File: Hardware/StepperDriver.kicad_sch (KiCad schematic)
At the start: 0 parts

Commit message: Initial schematic
Completed the first iteration for the schematic.
Included a default 42x42mm PCB area.
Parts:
- added C1, C3, C4: 22u, Capacitor_SMD:C_1206_3216Metric, symbol Device:C
- added C10, C11, C15, C16, C17, C18, C20, C21, C6, C9: 100n, Capacitor_SMD:C_0603_1608Metric, symbol Device:C
- added C12, C19, C2, C8: 10n, Capacitor_SMD:C_0603_1608Metric, symbol Device:C
- added C13: 2.2u, Capacitor_SMD:C_0603_1608Metric, symbol Device:C
- added C14: 100u, Capacitor_SMD:CP_Elec_8x10.5, symbol Device:C_Polarized
- added C5: 22n, Capacitor_SMD:C_0603_1608Metric, symbol Device:C
- added C7: 1u, Capacitor_SMD:C_0603_1608Metric, symbol Device:C
- added D1, D2: SS210, Diode_SMD:D_SMA, symbol Device:D_Schottky
- added J1: LCD, Custom_Parts:OLED_128X32_0.91, symbol Connector_Generic:Conn_01x04
- added J2: JTAG, Connector_PinHeader_1.27mm:PinHeader_2x05_P1.27mm_Vertical, symbol Connector:Conn_ARM_JTAG_SWD_10
- added J3: UART, Connector_JST:JST_SH_SM03B-SRSS-TB_1x03-1MP_P1.00mm_Horizontal, symbol Connector_Generic_MountingPin:Conn_01x03_MountingPin
- added J4: MOTOR, Connector_PinHeader_2.54mm:PinHeader_1x04_P2.54mm_Vertical, symbol Connector_Generic:Conn_01x04
- added L1: 47u, Inductor_SMD:L_Changjiang_FNR5040S, symbol Device:L
- added R1, R2: 2.2K, Resistor_SMD:R_0603_1608Metric, symbol Device:R
- added R10, R12, R13, R15, R16, R6, R9: 10K, Resistor_SMD:R_0603_1608Metric, symbol Device:R
- added R11, R14: 100m, Resistor_SMD:R_1206_3216Metric, symbol Device:R
- added R3, R4: 100, Resistor_SMD:R_0603_1608Metric, symbol Device:R
- added R5: 1K, Resistor_SMD:R_0603_1608Metric, symbol Device:R
- added R7: 3.3K, Resistor_SMD:R_0603_1608Metric, symbol Device:R
- added R8: 22K, Resistor_SMD:R_0603_1608Metric, symbol Device:R
- added SW1: SW_M, Button_Switch_SMD:SW_SPST_TS-1088-xR020, symbol Switch:SW_Push
- added SW2: SW_C, Button_Switch_SMD:SW_SPST_TS-1088-xR020, symbol Switch:SW_Push
- added SW3: SW_P, Button_Switch_SMD:SW_SPST_TS-1088-xR020, symbol Switch:SW_Push
- added U1: TPS5430DDA, Custom_Parts:TI_SO-PowerPAD-8_ThermalVias, symbol Regulator_Switching:TPS5430DDA
- added U2: XIAO-RP2350, Custom_Parts:XIAO-RP2350-SMD, symbol Custom_Parts:XIAO-RP2350-SMD
- added U3: TMC2208-LA, Custom_Parts:QFN-28-1EP_5x5mm_P0.5mm_EP3.1x3.1mm_ThermalVias, symbol Driver_Motor:TMC2208-LA
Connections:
- new net: R12.2, R13.2, SW2.1
- new net: R15.2, R16.2, SW3.1
- new net: R10.2, R9.2, SW1.1
- new net +3V3: C9.1, J1.3 (Pin_3), J2.1 (VTref), R1.1, R10.1, R13.1, R16.1, R2.1, U2.12 (3V3), U2.26 (3V3), U3.15 (VCC_IO)
- new net +5V: C3.1, C4.1, L1.2, R6.1, U2.14 (VBUS)
- new net +VDC: C10.1, C11.1, C14.1, C6.1, D1.2 (A), U3.22 (VS), U3.28 (VS)
- new net BOOT: C2.1, U1.1 (BOOT)
- new net CLK: J2.4 (SWCLK/TCK), R3.2
- new net CPI: C5.2, U3.5 (CPI)
- new net CPO: C5.1, U3.4 (CPO)
- new net DIO: J2.2 (SWDIO/TMS), R4.1
- new net DRV_DIAG: U2.18 (GPIO16_SDA0), U3.11 (DIAG)
- new net DRV_DIR: U2.1 (GPIO26_A0), U3.19 (DIR)
- new net DRV_EN: U2.4 (GPIO5_SPI0_CS), U3.2 (~{EN})
- new net DRV_INDEX: U2.17 (GPIO17_SCL0), U3.12 (INDEX)
- new net DRV_STEP: U2.2 (GPIO27_A1), U3.16 (STEP)
- new net DRV_UART: R5.1, U2.8 (GPIO1_RX0), U3.14 (~{PD}/UART)
- new net DRV_VREF: R8.1, U2.3 (GPIO28_A2)
- new net GND: C1.2, C10.2, C11.2, C12.2, C13.2, C14.2, C15.2, C16.2, C17.2, C18.2, C19.2, C20.2, C21.2, C3.2, C4.2, C7.2, C8.2, C9.2, D2.2 (A), J1.4 (Pin_4), J2.3 (GND), J2.5 (GND), J2.9 (GNDDetect), J3.2 (Pin_2), R11.2, R14.2, R7.2, SW1.2, SW2.2, SW3.2, U1.6 (GND), U1.9 (GNDPAD), U2.13 (GND), U2.27 (GND), U2.30 (GND), U3.13 (CLK), U3.18 (GND), U3.29 (GND), U3.3 (GND)
- new net M_A1: C15.1, J4.4 (Pin_4), U3.24 (OA1)
- new net M_A2: C17.1, J4.3 (Pin_3), U3.21 (OA2)
- new net M_B1: C18.1, J4.2 (Pin_2), U3.26 (OB1)
- new net M_B2: C20.1, J4.1 (Pin_1), U3.1 (OB2)
- new net RST: J2.10 (~{RESET}), U2.24 (RST)
- new net SCL: J1.2 (Pin_2), R1.2, U2.6 (GPIO7_SCL1)
- new net SDA: J1.1 (Pin_1), R2.2, U2.5 (GPIO6_SDA1)
- new net SNSA: C16.1, R11.1, U3.23 (BRA)
- new net SNSB: C21.1, R14.1, U3.27 (BRB)
- new net SWCLK: R3.1, U2.28 (SWDCLK)
- new net SWDIO: R4.2, U2.23 (SWDIO)
- new net SW_C: C12.1, R12.1, U2.10 (GPIO4_SPI0_MISO)
- new net SW_M: C8.1, R9.1, U2.9 (GPIO2_SPI0_SCK)
- new net SW_P: C19.1, R15.1, U2.11 (GPIO3_SPI0_MOSI)
- new net TX: R5.2, U2.7 (GPIO0_TXO)
- new net UART_RX: J3.1 (Pin_1), U2.15 (GPIO21_RX1)
- new net UART_TX: J3.3 (Pin_3), U2.16 (GPIO20_TX1)
- new net VCP: C6.2, U3.6 (VCP)
- new net VDC_PROT: C1.1, D1.1 (K), U1.7 (VIN)
- new net VOUT: C13.1, U3.8 (5VOUT)
- new net VREF: C7.1, R8.2, U3.17 (VREF)
- new net VSNS: R6.2, R7.1, U1.4 (VSENSE)
- new net VSW: C2.2, D2.1 (K), L1.1, U1.8 (PH)
- no-connect marks 0 -> 12

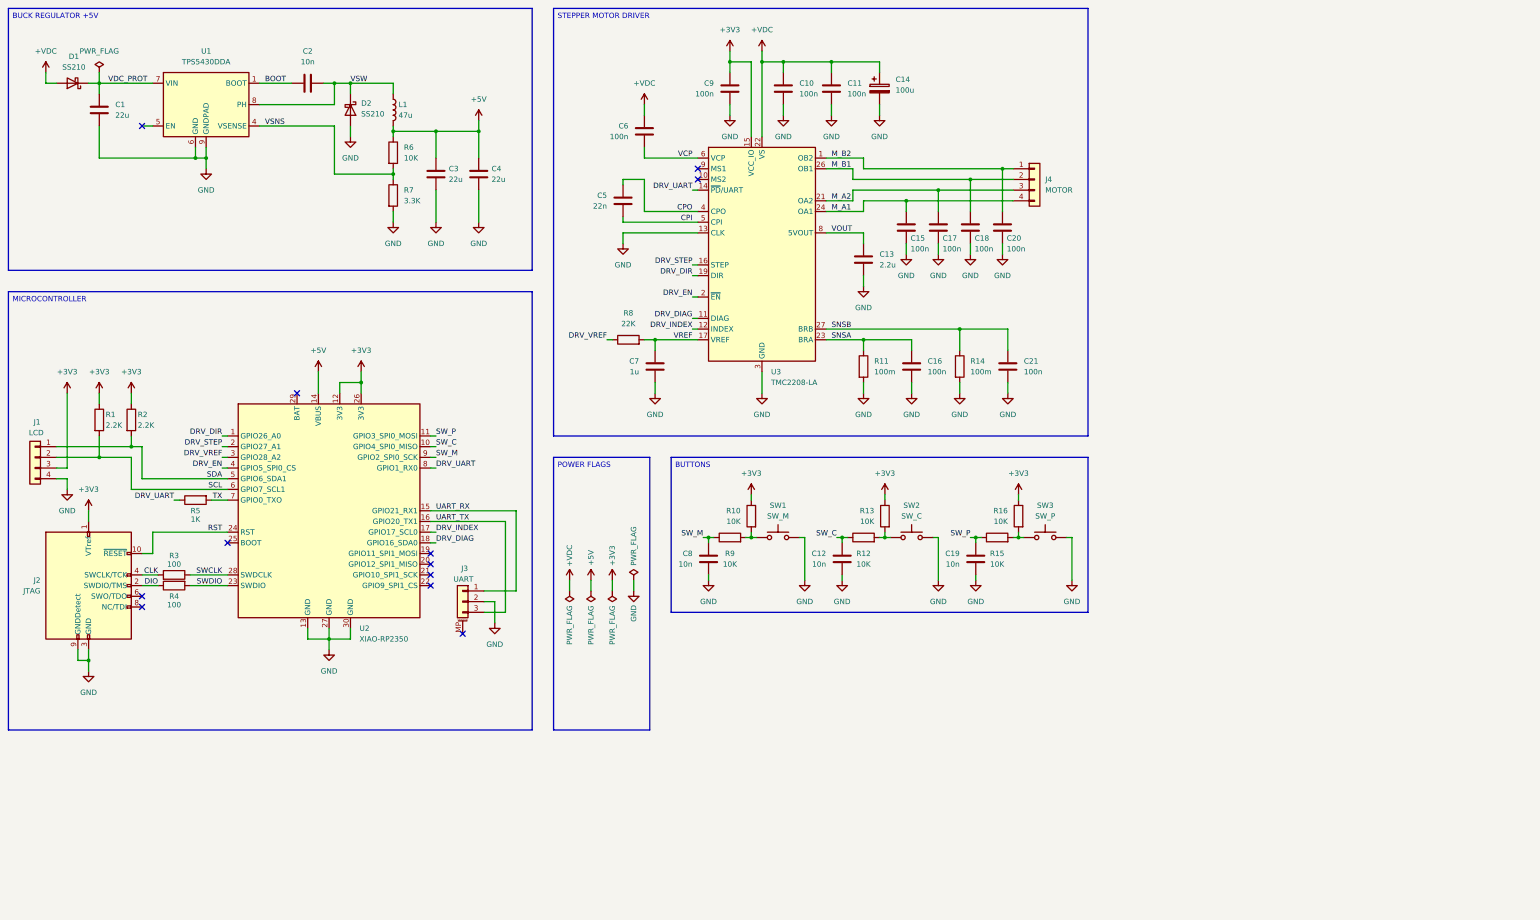
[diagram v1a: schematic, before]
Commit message: Initial layout
Completed the first iteration for the layout.
Increased the PCB area to 50x50mm.
Minor changes in the schematic.
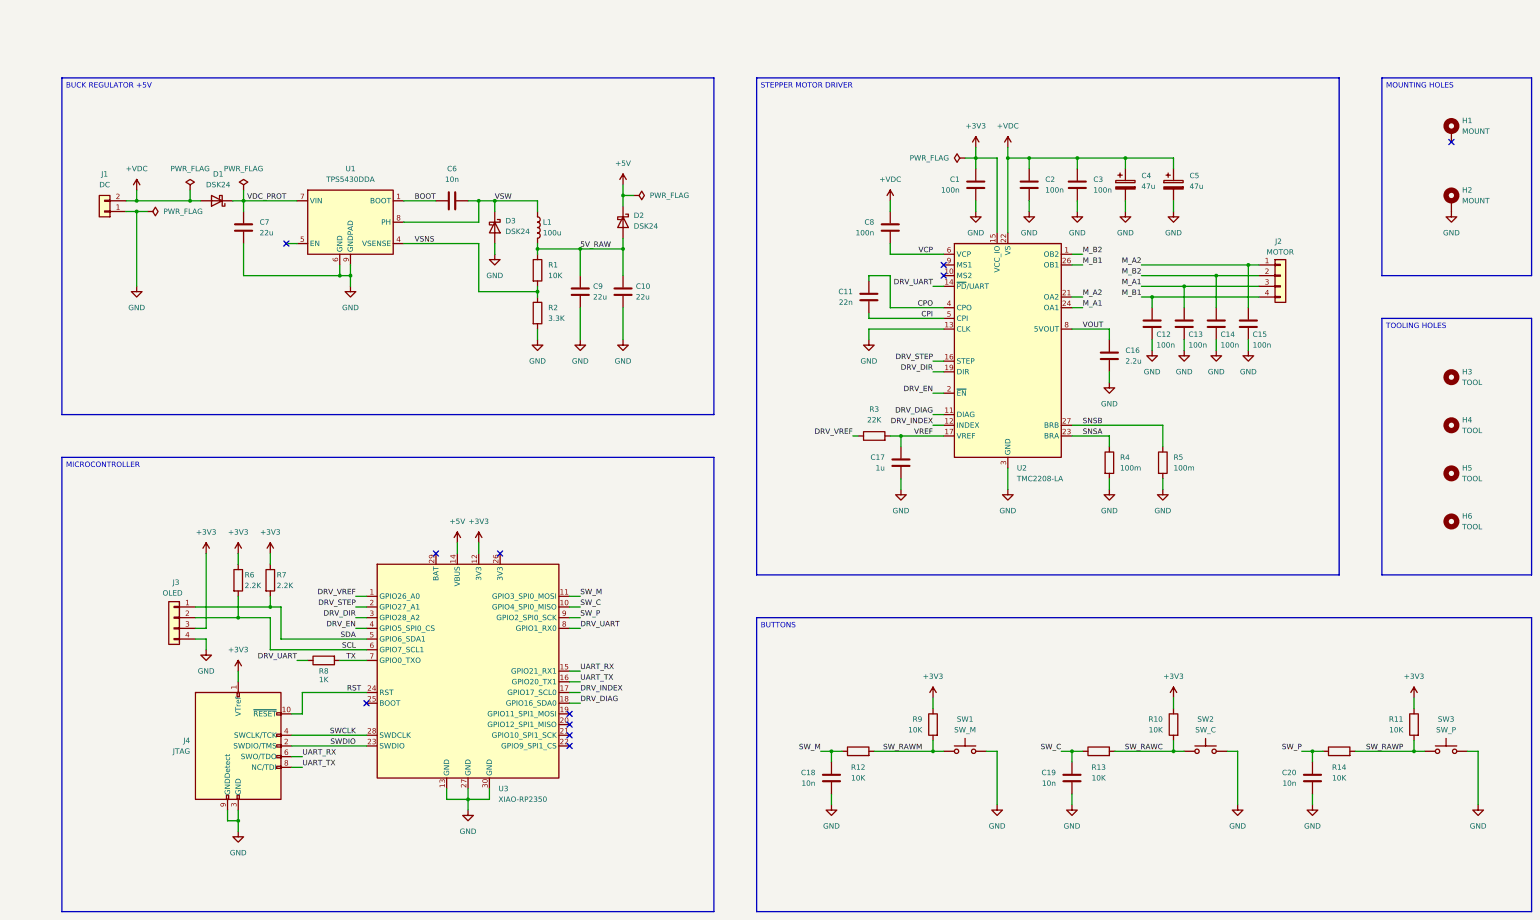
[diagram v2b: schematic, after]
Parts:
- removed C16, C21: 100n, Capacitor_SMD:C_0603_1608Metric, symbol Device:C
- removed J3: UART, Connector_JST:JST_SH_SM03B-SRSS-TB_1x03-1MP_P1.00mm_Horizontal, symbol Connector_Generic_MountingPin:Conn_01x03_MountingPin
- removed R3, R4: 100, Resistor_SMD:R_0603_1608Metric, symbol Device:R
- added C5: 47u, Capacitor_SMD:CP_Elec_6.3x5.4, symbol Device:C_Polarized
- added D2: DSK24, Diode_SMD:D_SOD-123F, symbol Device:D_Schottky
- added H1, H2: MOUNT, MountingHole:MountingHole_3.2mm_M3_Pad_Via, symbol Mechanical:MountingHole_Pad
- added H3, H4, H5, H6: TOOL, MountingHole:ToolingHole_1.152mm, symbol Mechanical:MountingHole
- added J1: DC, Custom_Parts:JST_PH_S2B_1x02_COMBO, symbol Connector_Generic:Conn_01x02
- C4: renamed from C14; value 100u -> 47u; footprint Capacitor_SMD:CP_Elec_8x10.5 -> Capacitor_SMD:CP_Elec_6.3x5.4
- D1: value SS210 -> DSK24; footprint Diode_SMD:D_SMA -> Diode_SMD:D_SOD-123F
- D3: renamed from D2; value SS210 -> DSK24; footprint Diode_SMD:D_SMA -> Diode_SMD:D_SOD-123F
- J2: renamed from J4; footprint Connector_PinHeader_2.54mm:PinHeader_1x04_P2.54mm_Vertical -> Custom_Parts:JST_PH_S4B_1x04_COMBO
- J3: renamed from J1; value LCD -> OLED; footprint Custom_Parts:OLED_128X32_0.91 -> Custom_Parts:OLED_128X32_0.91_HEADER
- L1: value 47u -> 100u
- renumbered C9 to C1, C4 to C10, C5 to C11, C15 to C12, C17 to C13, C18 to C14, C20 to C15, C13 to C16, C7 to C17, C8 to C18, C12 to C19, C10 to C2, C19 to C20, C11 to C3, C2 to C6, C1 to C7, C6 to C8, C3 to C9, J2 to J4, R6 to R1, R13 to R10, R16 to R11, R9 to R12, R12 to R13, R15 to R14, R7 to R2, R8 to R3, R11 to R4, R14 to R5, R1 to R6, R2 to R7, R5 to R8, R10 to R9, U3 to U2, U2 to U3
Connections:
- net CLK is gone; now on net SWCLK: J4.4 (SWCLK/TCK)
- net DIO is gone; now on net SWDIO: J4.2 (SWDIO/TMS)
- net +3V3: no longer U3.26 (3V3)
- net +5V: now also D2.1 (K); no longer C10.1, C9.1, L1.2, R1.1
- net +VDC: now also C5.1, J1.2 (Pin_2)
- net DRV_DIR: now also U3.3 (GPIO28_A2); no longer U3.1 (GPIO26_A0)
- net DRV_VREF: now also U3.1 (GPIO26_A0); no longer U3.3 (GPIO28_A2)
- net GND: now also C5.2, H2.1, J1.1 (Pin_1)
- net M_A1: now also C13.1, J2.3 (Pin_3); no longer C12.1, J2.4 (Pin_4)
- net M_A2: now also C15.1, J2.1 (Pin_1); no longer C13.1, J2.3 (Pin_3)
- net M_B1: now also C12.1, J2.4 (Pin_4); no longer C14.1, J2.2 (Pin_2)
- net M_B2: now also C14.1, J2.2 (Pin_2); no longer C15.1, J2.1 (Pin_1)
- net SW_M: now also U3.11 (GPIO3_SPI0_MOSI); no longer U3.9 (GPIO2_SPI0_SCK)
- net SW_P: now also U3.9 (GPIO2_SPI0_SCK); no longer U3.11 (GPIO3_SPI0_MOSI)
- net UART_RX: now also J4.6 (SWO/TDO)
- net UART_TX: now also J4.8 (NC/TDI)
- net SW_RAWC: now reaches R10.2, R13.2, SW2.1
- net SW_RAWP: now reaches R11.2, R14.2, SW3.1
- net SW_RAWM: now reaches R12.2, R9.2, SW1.1
- new net 5V_RAW: C10.1, C9.1, D2.2 (A), L1.2, R1.1
- no-connect marks 12 -> 11
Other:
- moved on the sheet: C1, C10, C11, C12, C13, C14, C15, C16, C17, C18, C19, C2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

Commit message: Initial ESP32C6 layout
Moved to a XIAO ESP32C6 development board.
Completed the first iteration for the layout.
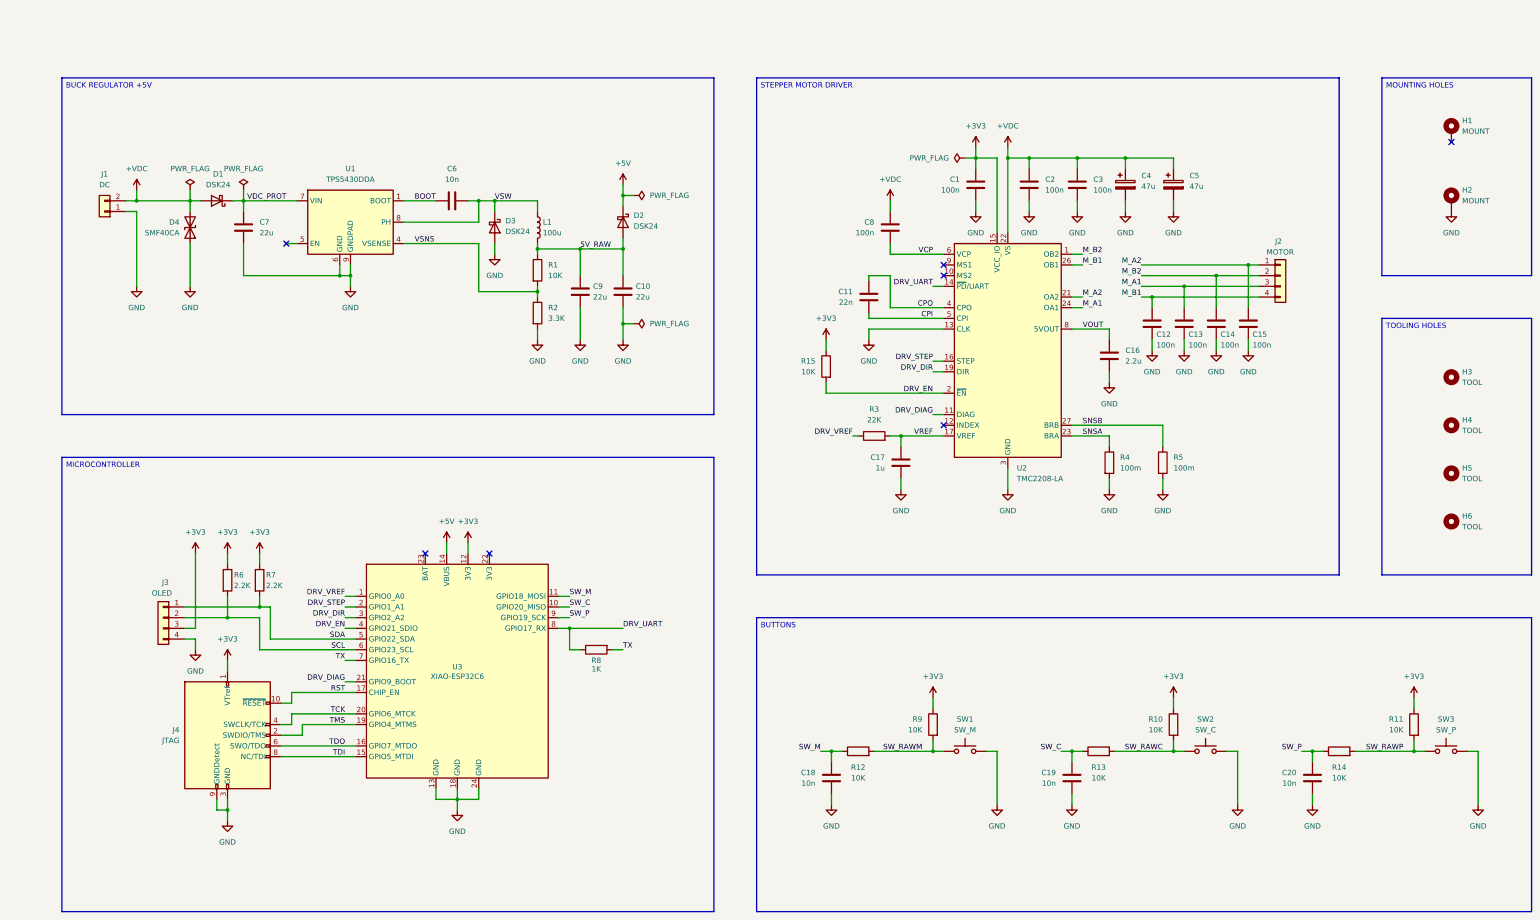
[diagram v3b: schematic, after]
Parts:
- removed U3: XIAO-RP2350, Custom_Parts:XIAO-RP2350-SMD, symbol Custom_Parts:XIAO-RP2350-SMD
- added D4: SMF40CA, Diode_SMD:D_SOD-123F, symbol Device:D_TVS
- added R15: 10K, Resistor_SMD:R_0603_1608Metric, symbol Device:R
- added U3: XIAO-ESP32C6, Custom_Parts:XIAO-ESP32C6-SMD, symbol Custom_Parts:XIAO-ESP32C6-SMD
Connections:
- net +3V3: now also R15.1, U3.12 (3V3)
- net +5V: now also U3.14 (VBUS)
- net +VDC: now also D4.2 (A2)
- net DRV_DIAG: now also U3.21 (GPIO9_BOOT)
- net DRV_DIR: now also U3.3 (GPIO2_A2)
- net DRV_EN: now also R15.2, U3.4 (GPIO21_SDIO)
- net DRV_STEP: now also U3.2 (GPIO1_A1)
- net DRV_UART: now also U3.8 (GPIO17_RX)
- net DRV_VREF: now also U3.1 (GPIO0_A0)
- net GND: now also D4.1 (A1), U3.13 (GND), U3.18 (GND), U3.24 (GND)
- net RST: now also U3.17 (CHIP_EN)
- net SCL: now also U3.6 (GPIO23_SCL)
- net SDA: now also U3.5 (GPIO22_SDA)
- net SW_C: now also U3.10 (GPIO20_MISO)
- net SW_M: now also U3.11 (GPIO18_MOSI)
- net SW_P: now also U3.9 (GPIO19_SCK)
- net TX: now also U3.7 (GPIO16_TX)
- net DRV_INDEX: no longer names the net of U2.12 (INDEX)
- net SWCLK renamed TCK
- net TCK: now also U3.20 (GPIO6_MTCK)
- net SWDIO renamed TMS
- net TMS: now also U3.19 (GPIO4_MTMS)
- net UART_RX renamed TDO
- net TDO: now also U3.16 (GPIO7_MTDO)
- net UART_TX renamed TDI
- net TDI: now also U3.15 (GPIO5_MTDI)
- no-connect marks 11 -> 7
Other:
- moved on the sheet: J3, J4, R6, R7

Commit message: Build output files
Generated the output files for the first iteration of the ESP32-C6 board.
Added some board images and 3D model.
Added the BOM and POS files for assembly.
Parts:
- added FID1, FID2, FID3: FIDUCIAL, Fiducial:Fiducial_0.75mm_Mask1.5mm, symbol Mechanical:Fiducial
- C1, C12, C13, C14, C15, C2, C3, C8: JLCPCB Part (none) -> C14663; Manufacturer Part (none) -> CC0603KRX7R9BB104
- C10, C9: JLCPCB Part (none) -> C12891; Manufacturer Part (none) -> CL31A226KAHNNNE
- C11: JLCPCB Part (none) -> C21122; Manufacturer Part (none) -> CL10B223KB8NNNC
- C16: JLCPCB Part (none) -> C23630; Manufacturer Part (none) -> CL10A225KO8NNNC
- C17: JLCPCB Part (none) -> C15849; Manufacturer Part (none) -> CL10A105KB8NNNC
- C18, C19, C20, C6: JLCPCB Part (none) -> C57112; Manufacturer Part (none) -> 0603B103K500NT
- C4, C5: JLCPCB Part (none) -> C44606723; Manufacturer Part (none) -> SM476M050E0800
- C7: value 22u -> 10u; JLCPCB Part (none) -> C13585; Manufacturer Part (none) -> CL31A106KBHNNNE
- D1, D2, D3: JLCPCB Part (none) -> C22466352; Manufacturer Part (none) -> DSK24
- D4: JLCPCB Part (none) -> C42371749; Manufacturer Part (none) -> SMF40CA
- H1, H2, H3, H4, H5, H6: JLCPCB Part (none) -> -; Manufacturer Part (none) -> -
- J1: JLCPCB Part (none) -> C265016; Manufacturer Part (none) -> S2B-PH-K(LF)(SN); now left out of the parts list
- J2: JLCPCB Part (none) -> C265452; Manufacturer Part (none) -> S4B-PH-K(LF)(SN); now left out of the parts list
- J3: footprint Custom_Parts:OLED_128X32_0.91_HEADER -> Custom_Parts:HEADER_THROUGH_1x04_P2.54mm; JLCPCB Part C2691448 -> -; Manufacturer Part PZ254V-11-04P -> -
- J4, U3: JLCPCB Part (none) -> -; Manufacturer Part (none) -> -; now left out of the parts list
- L1: value 100u -> 47u; JLCPCB Part (none) -> C167974; Manufacturer Part (none) -> FNR5040S470MT
- R1, R10, R11, R12, R13, R14, R15, R9: JLCPCB Part (none) -> C25804; Manufacturer Part (none) -> 0603WAF1002T5E
- R2: JLCPCB Part (none) -> C22978; Manufacturer Part (none) -> 0603WAF3301T5E
- R3: JLCPCB Part (none) -> C31850; Manufacturer Part (none) -> 0603WAF2202T5E
- R4, R5: JLCPCB Part (none) -> C25334; Manufacturer Part (none) -> 1206W4F100LT5E
- R6, R7: JLCPCB Part (none) -> C4190; Manufacturer Part (none) -> 0603WAF2201T5E
- R8: JLCPCB Part (none) -> C21190; Manufacturer Part (none) -> 0603WAF1001T5E
- SW1, SW2, SW3: JLCPCB Part (none) -> C720477; Manufacturer Part (none) -> TS-1088-AR02016
- U1: JLCPCB Part (none) -> C9864; Manufacturer Part (none) -> TPS5430DDAR
- U2: JLCPCB Part (none) -> C115944; Manufacturer Part (none) -> TMC2208-LA-T
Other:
- moved on the sheet: H3, H4, H5, H6

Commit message: Assembly revision
Minor changes to the board and schematic.
Updated the output files.
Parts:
- SW1: value SW_M -> SPST_TS
- SW2: value SW_C -> SPST_TS
- SW3: value SW_P -> SPST_TS
- renumbered D4 to D3, D3 to D4, R9 to R10, R10 to R11, R11 to R12, R12 to R13, R13 to R14, R14 to R15, R15 to R3, R3 to R4, R4 to R5, R5 to R6, R6 to R7, R7 to R8, R8 to R9
